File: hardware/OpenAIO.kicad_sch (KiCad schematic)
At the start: 15 parts, among them J1 OpenDrone-Core, U1 AIO_outline, U19 INA186A3IDCKR

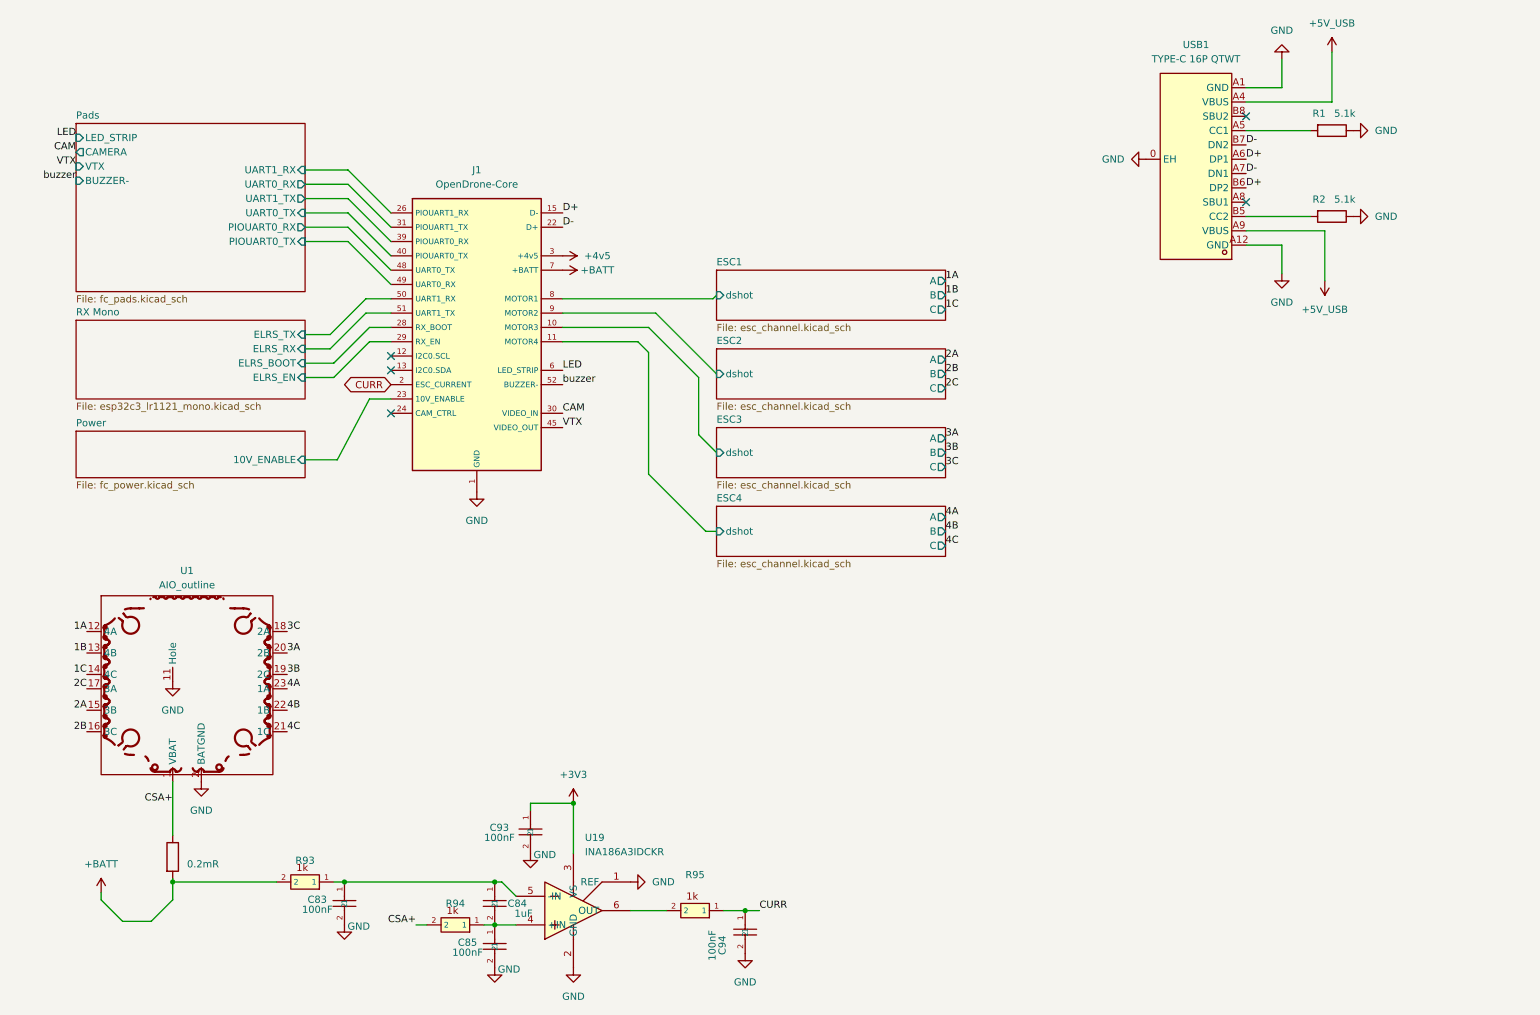
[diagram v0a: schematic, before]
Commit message: One board: Base + Core merged on the 8L HDI stackup, replaces the OpenFC-Core module layout (#25)
* Base fully routed (recovered from KiCad local history, 2026-08-22)

The finished Base route was never committed: the last Base commit (ce0aa59)
had 57 unconnected. Recovered from hardware/.history snapshot 55d048e
(last save 2026-08-22 15:03), on top of ce0aa59.

DRC (kicad-cli 10):
- Base: 0 unconnected, 0 shorts, 6 errors (3 x U23 own pad-to-pad
  clearance, USB1 NPTH: 1 clearance + 2 annular width), 111 warnings
- Core: 0 unconnected, 0 errors

Co-Authored-By: Claude Opus 5.5 <noreply@anthropic.com>

* Power: +10V buck always on with battery, 10V_ENABLE removed

CIRCUIT_REVIEW B1: the LMR51430 +10V buck U3 (NSG2065Q gate drive and VTX power) was enabled by RP2354A GPIO27 over LGA pad 1 with no pull, so firmware or a Betaflight PINIO could cut ESC gate drive, and on USB-only power a high GPIO27 drove EN with VIN = 0, which the LMR51430 datasheet forbids. U3 EN is now tied to +BATT exactly like U4 (datasheet: EN may be tied to VIN; no parts added). Base: U3.5 keeps its B.Cu stub and through via, re-netted to +BATT so the via lands in the +BATT planes; the In2 run, the via and the F.Cu stub to J90 pad 1 are removed. Core: the GPIO27 route to J91 pad 1 is removed. LGA pad 1 and GPIO27 are free (no-connect); the root marker TP14 of the old net is dropped. Boards saved by pcbnew 10.0.6 without zone refill; the "Tokyo" silkscreen render caches were re-rendered with a substitute font (Tokyo not installed here).

Co-Authored-By: Claude Opus 5.5 <noreply@anthropic.com>
Claude-Session: https://claude.ai/code/session_01KTp3FLjVXfXdWrkmr6af7d

* Review of the split Core/Base design, NextPCB rules, re-route plan

Circuit review against datasheets, layout review (LGA interface, DC power
solver, noise, density, assembly, DRC) with the scripts that produced every
number, NextPCB fab and assembly limits with sources, and the plan with the
decisions taken for the re-route.

Co-Author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
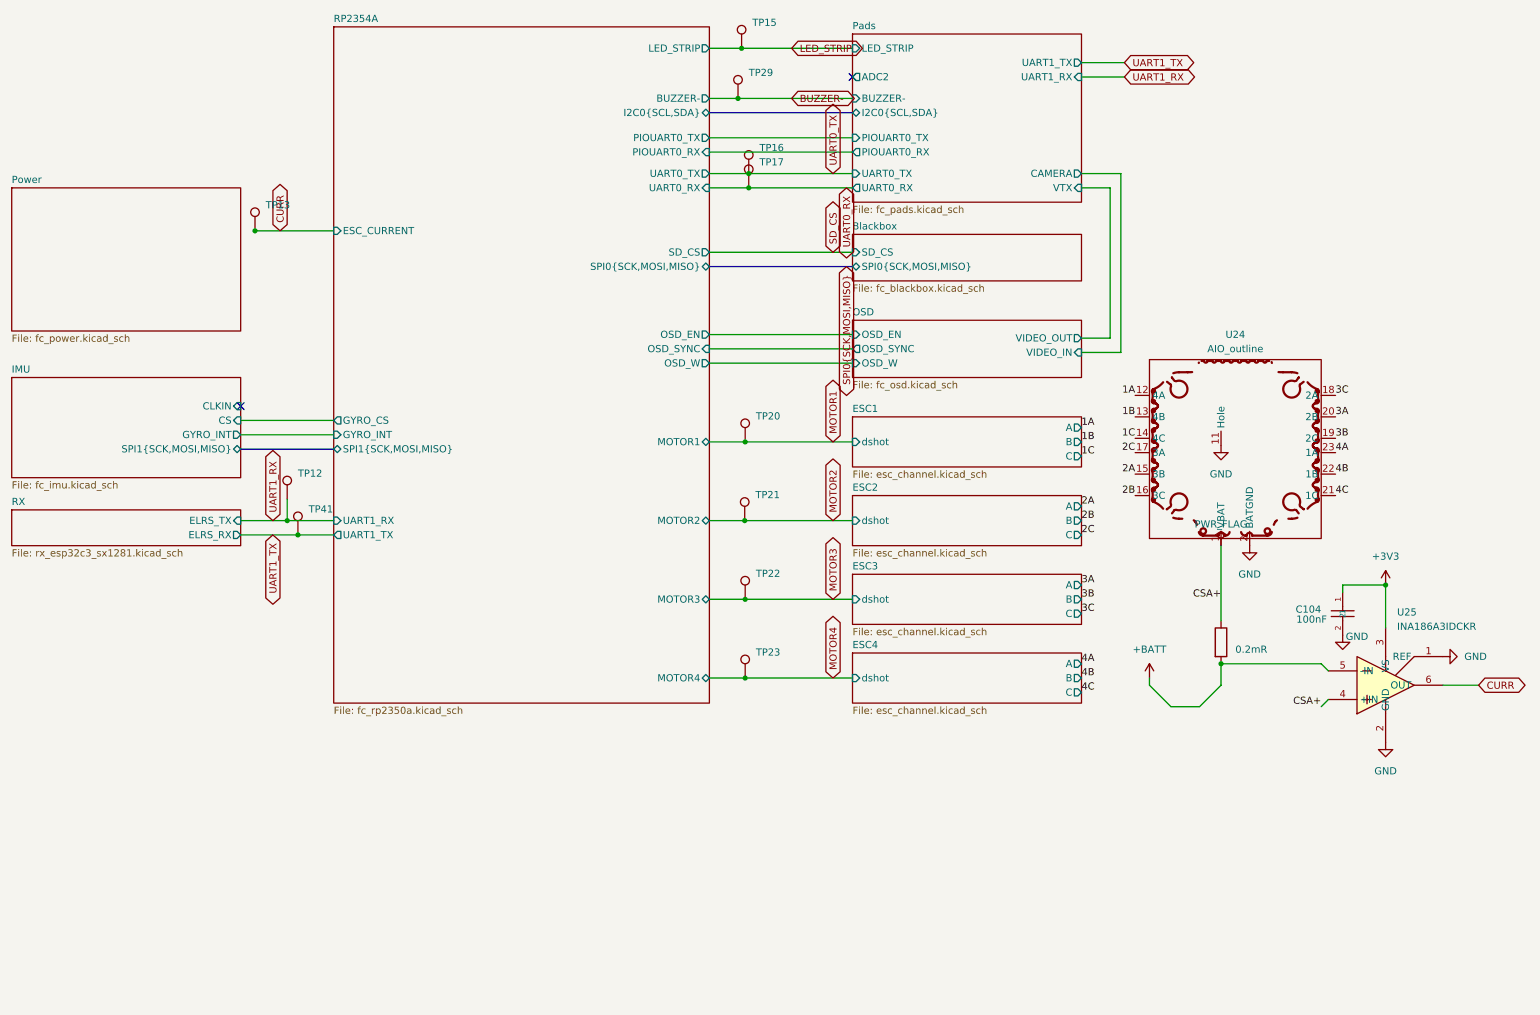
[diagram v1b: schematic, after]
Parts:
- removed C83, C85: 100nF, Capacitor_SMD:C_0402_WIDE, symbol ESCLibrary:GRM033R61C104KE84D
- removed C84: 1uF, Capacitor_SMD:C_0402_1005Metric, symbol ESCLibrary:GRM033R61C104KE84D
- removed C93, C94: 100nF, Capacitor_SMD:C_0201_0603Metric, symbol ESCLibrary:GRM033R61C104KE84D
- removed J1: OpenDrone-Core, lib:OpenDrone-Core_LGA_land, symbol lib:OpenDrone-Core
- removed R1, R2: 5.1k, Resistor_SMD:R_0201_0603Metric, symbol Device:R
- removed R93, R94: 1k, Capacitor_SMD:C_0201_0603Metric, symbol components:0201_1kR
- removed R95: 1k, 4in1ESC:R_0201_0603Metric, symbol ESCLibrary:0201_1kR
- removed U19: INA186A3IDCKR, 4in1ESC:SOT-363_SC-70-6, symbol components:INA186A3IDCKR
- removed USB1: TYPE-C 16P QTWT, lib:USB-TYPE-C-SMD_TYPE-C-16P-QTWT, symbol lib:TYPE-C16PQTWT
- added C104: 100nF, lib:C_0201_0603Metric, symbol lib:GRM033R61C104KE84D
- added TP12, TP13, TP15, TP16, TP17, TP20, TP21, TP22, TP23, TP29, TP41: TestPoint, lib:TestPoint_Pad_D1.0mm, symbol Connector:TestPoint
- added U25: INA186A3IDCKR, lib:SOT-363_SC-70-6, symbol lib:INA186A3IDCKR
- Rsense2: footprint Resistor_SMD:R_2512_6332Metric -> lib:R_2512_6332Metric; KiLib_Generator (none) -> SMD_2terminal_chip_molded; Manufacturer Yezhan -> (none)
- U24: renamed from U1; footprint OpenDrone:AIO_outline -> lib:AIO_outline; now left out of the parts list
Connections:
- net +3V3: now also C104.1, U25.3 (VS)
- net +BATT: now also U25.5 (-IN)
- net CSA+: now also U25.4 (+IN)
- net CURR: now also TP13.1, U25.6 (OUT)
- net GND: now also C104.2, U25.1 (REF), U25.2 (GND)
- new net BUZZER-: TP29.1
- new net LED_STRIP: TP15.1
- new net MOTOR1: TP20.1
- new net MOTOR2: TP21.1
- new net MOTOR3: TP22.1
- new net MOTOR4: TP23.1
- new net UART0_RX: TP17.1
- new net UART0_TX: TP16.1
- new net UART1_RX: TP12.1
- new net UART1_TX: TP41.1
- no-connect marks 5 -> 2
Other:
- removed sheet RX Mono
- added sheet Blackbox (fc_blackbox.kicad_sch)
- added sheet IMU (fc_imu.kicad_sch)
- added sheet OSD (fc_osd.kicad_sch)
- added sheet RP2354A (fc_rp2350a.kicad_sch)
- added sheet RX (rx_esp32c3_sx1281.kicad_sch)
- sheet Pads ports: added ADC2, I2C0{SCL,SDA}; removed none
- sheet Power ports: added none; removed 10V_ENABLE
- title: (none) -> OpenAIO
- moved on the sheet: U24
